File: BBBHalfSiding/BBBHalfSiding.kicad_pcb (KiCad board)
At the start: 2 copper layers, 89.4 x 166.9 mm, 70 parts, among them IC1 MCT6H, J1 2 1 0, J2 RJ45, J3 RJ45, P1 In Track Out, P10 + 12 out -, P11 WP 1 0, P2 East (Points), P3 West Main (Frog, Normal), P4 ABS Slave Bus, P5 West Div. (Frog, Revesed), P6 Termination, P7 - 12 in +, P8 BeagleBone_Black_Header, P9 BeagleBone_Black_Header, T1 FMR FMY FMG PLR PLY PHR PHY P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, T2 SP7 SP6 SP5 SP4 SP3 FDR FDY F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, T4 Motor 0, T5 Motor 1, U1 MCP23017, U10 74LV125AN, U11 74LV125AN, U12 MCP2551, U13 CAT24C256W, U2 ULN2803A, U3 ULN2803A, U4 TC4428, U5 TC4428, U6 74HC00, U7 TRS202E, U8 SN75LBC179, U9 TRS202E

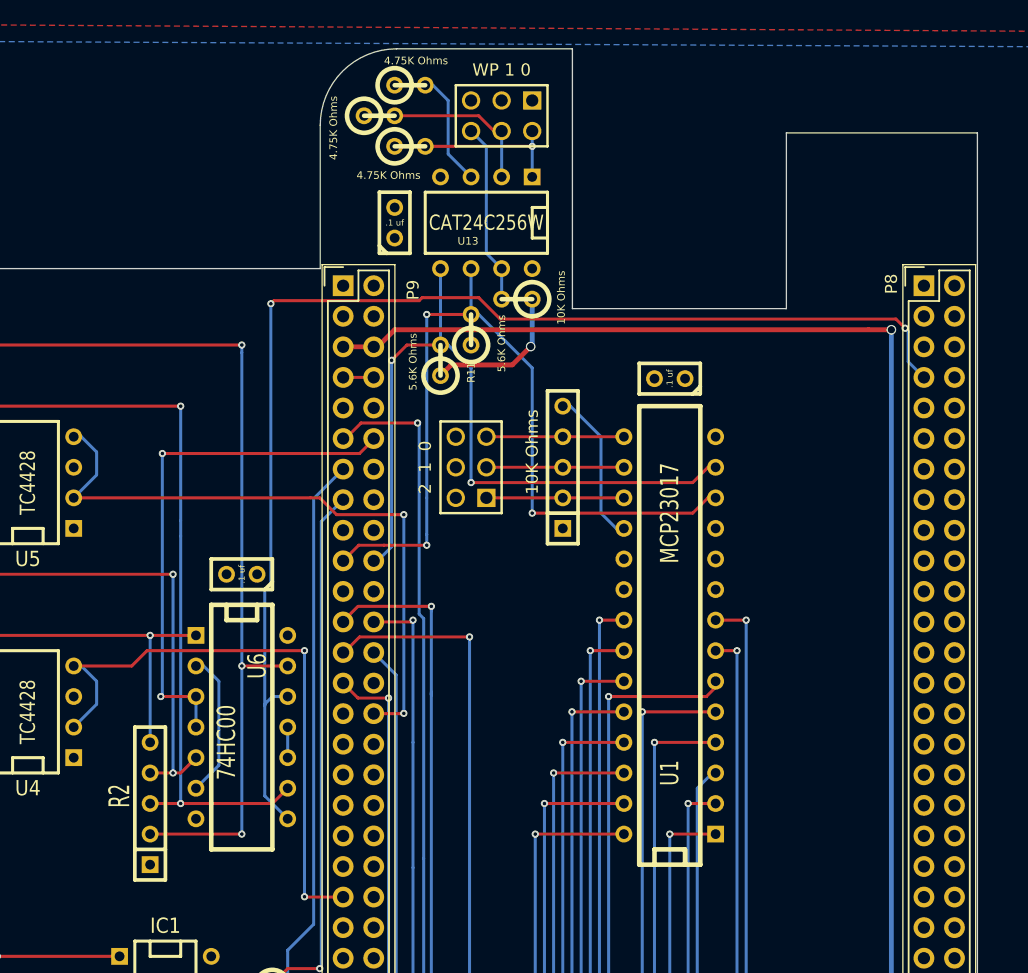
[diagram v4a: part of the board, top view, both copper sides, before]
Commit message: Tweaks to map to valid (unused) GPIO pins.
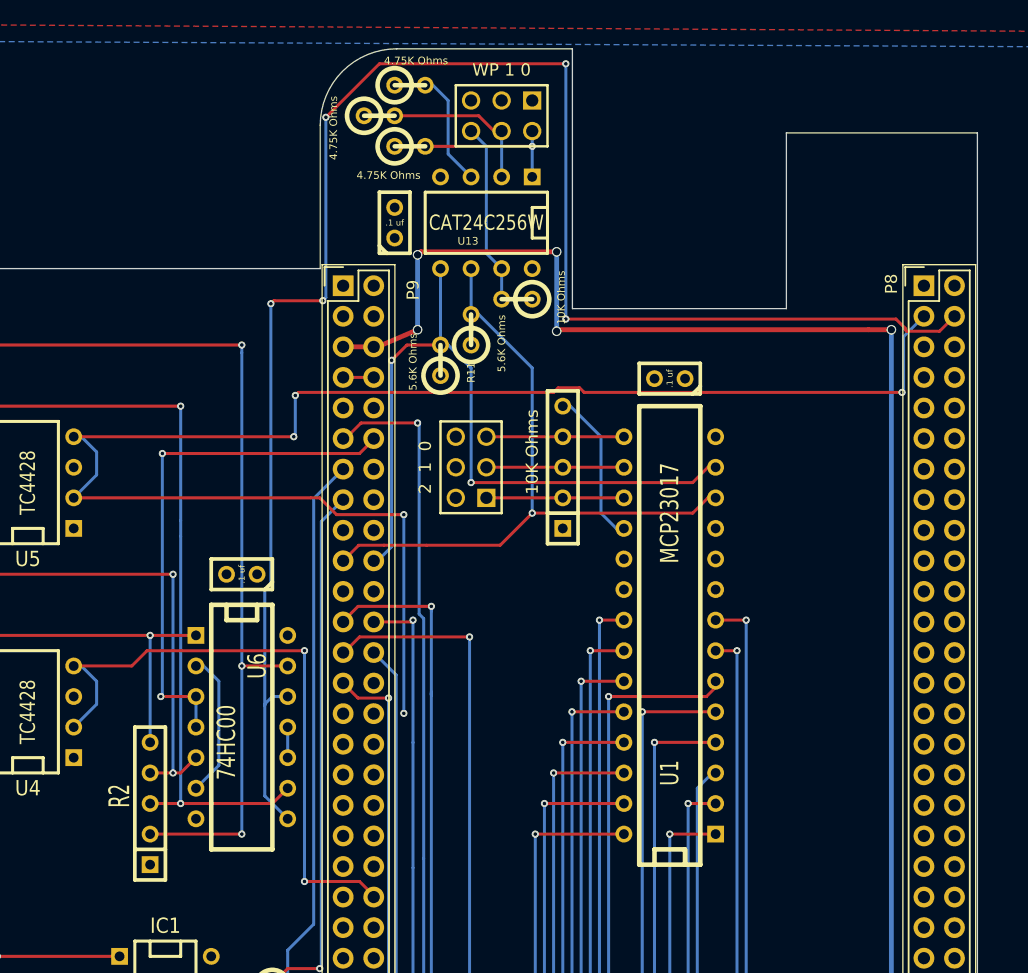
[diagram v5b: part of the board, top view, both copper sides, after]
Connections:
- P8 pad 3: (no net) -> /M1_Control
- P8 pad 4: (no net) -> /M1_Sense
- P8 pad 7: /M1_Sense -> (no net)
- P9 pad 30: /M1_Control -> (no net)
- P9 pad 41: /M0_Control -> (no net)
- P9 pad 42: (no net) -> /M0_Control
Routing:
- net /M1_Control: track 54.1 -> 131.3 mm, vias 2 -> 5
- net /M1_Sense: track 104.8 -> 142.3 mm, vias 2 -> 5
- net /Signals/SCL: track 68.9 -> 55.9 mm, vias 3 -> 1
- net +5V: track 274.3 -> 287.1 mm, vias 6 -> 10
- net +3.3V: track 12.5 -> 0.00 mm, vias 1 -> 0
- net /M0_Control: track 50.4 -> 52.3 mm
